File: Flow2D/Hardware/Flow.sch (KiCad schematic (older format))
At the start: 51 parts, among them J1 Conn_02x05_Odd_Even, U1 SN74LVC2G17, U2 LR9102G, U3 TLV9064IDR, U4 STM32G030F6Px

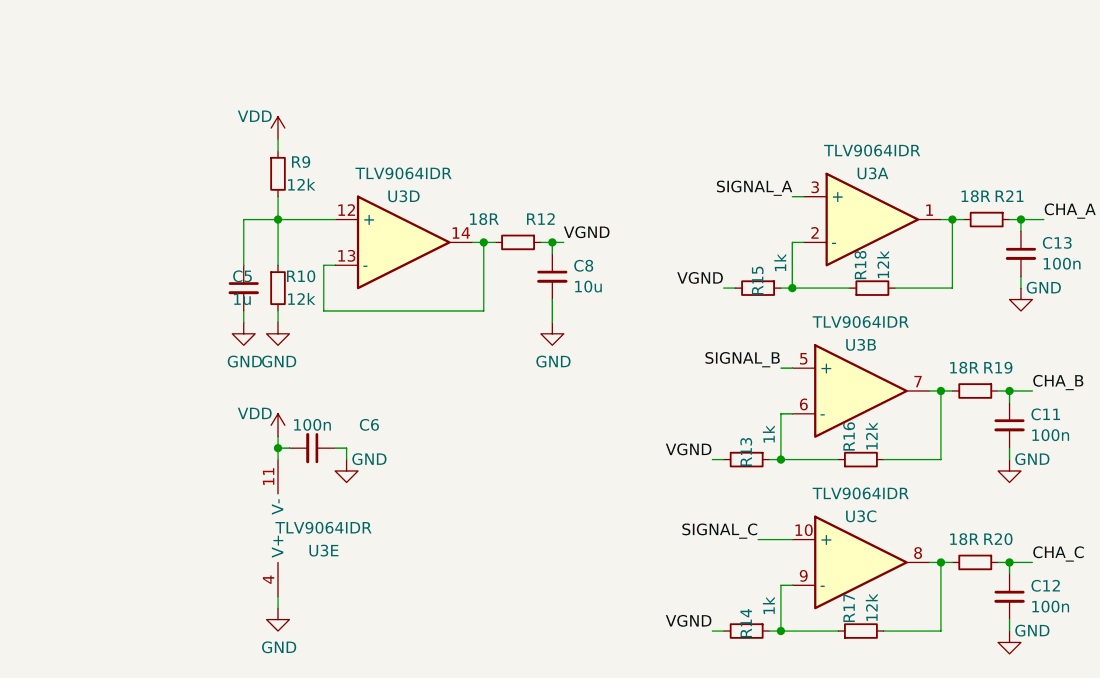
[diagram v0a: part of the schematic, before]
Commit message: Problems related to firmware are solved.
TODO:
+Signal level is too low; like 200mV. Need to be increased.
+Need to be tested with a plastic ring.
+Piezodriver units response is unknown, need to be determined.
+A bit more calculation about vectors required.
+No need for making DMA of the TIM1 active, could be deactivated.
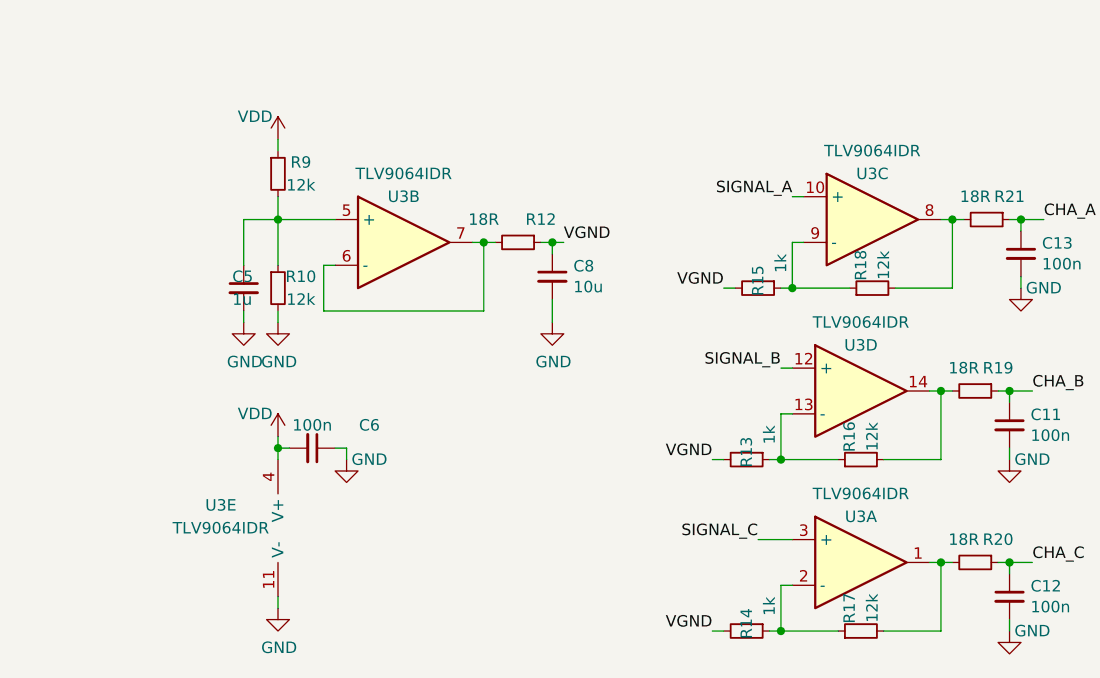
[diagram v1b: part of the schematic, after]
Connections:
- net GND: now also U3.11 (V-); no longer U3.4 (V+)
- net SIGNAL_A: now also U3.10 (+); no longer U3.3 (+)
- net SIGNAL_B: now also U3.12 (+); no longer U3.5 (+)
- net SIGNAL_C: now also U3.3 (+); no longer U3.10 (+)
- net VDD: now also U3.4 (V+); no longer U3.11 (V-)
- net at R16.2, R19.2: now also U3.14; no longer U3.7
- net at R17.2, R20.2: now also U3.1; no longer U3.8
- net at R13.1, R16.1: now also U3.13 (-); no longer U3.6 (-)
- net at R14.1, R17.1: now also U3.2 (-); no longer U3.9 (-)
- net at C5.1, R10.1, R9.2: now also U3.5 (+); no longer U3.12 (+)
- net at R18.2, R21.2: now also U3.8; no longer U3.1
- net at R15.1, R18.1: now also U3.9 (-); no longer U3.2 (-)
- new net: R12.2, U3.6 (-), U3.7
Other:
- moved on the sheet: U3A, U3B, U3C, U3D
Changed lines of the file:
@@
 L Device:Opamp_Quad_Generic U3
 U 4 1 60F6CC8E
-P 6950 7450
-F 0 "U3" H 6950 7650 50  0000 C CNN
-F 1 "TLV9064IDR" H 6950 7750 50  0000 C CNN
-F 2 "Package_SO:SOIC-14_3.9x8.7mm_P1.27mm" H 6950 7450 50  0001 C CNN
-F 3 "~" H 6950 7450 50  0001 C CNN
-F 4 "https://ozdisan.com/entegre-devreler-ics/lineer-entegreler/amplifikatorler/TLV9064IDR" H 6950 7450 50  0001 C CNN "Link"
-F 5 "0.77646" H 6950 7450 50  0001 C CNN "Price"
-	4    6950 7450
+P 8950 8100
+F 0 "U3" H 8950 8300 50  0000 C CNN
+F 1 "TLV9064IDR" H 8950 8400 50  0000 C CNN
+F 2 "Package_SO:SOIC-14_3.9x8.7mm_P1.27mm" H 8950 8100 50  0001 C CNN
+F 3 "~" H 8950 8100 50  0001 C CNN
+F 4 "https://ozdisan.com/entegre-devreler-ics/lineer-entegreler/amplifikatorler/TLV9064IDR" H 8950 8100 50  0001 C CNN "Link"
+F 5 "0.77646" H 8950 8100 50  0001 C CNN "Price"
+	4    8950 8100
 	1    0    0    -1
 $EndComp
@@
 L Device:Opamp_Quad_Generic U3
 U 5 1 60F6DBAD
-P 6500 8700
-F 0 "U3" H 6600 8800 50  0000 C CNN
-F 1 "TLV9064IDR" H 6600 8700 50  0000 C CNN
-F 2 "Package_SO:SOIC-14_3.9x8.7mm_P1.27mm" H 6500 8700 50  0001 C CNN
-F 3 "~" H 6500 8700 50  0001 C CNN
-F 4 "https://ozdisan.com/entegre-devreler-ics/lineer-entegreler/amplifikatorler/TLV9064IDR" H 6500 8700 50  0001 C CNN "Link"
-F 5 "0.77646" H 6500 8700 50  0001 C CNN "Price"
-	5    6500 8700
-	1    0    0    1
+P 6300 8700
+F 0 "U3" H 6450 8800 50  0000 C CNN
+F 1 "TLV9064IDR" H 6450 8700 50  0000 C CNN
+F 2 "Package_SO:SOIC-14_3.9x8.7mm_P1.27mm" H 6300 8700 50  0001 C CNN
+F 3 "~" H 6300 8700 50  0001 C CNN
+F 4 "https://ozdisan.com/entegre-devreler-ics/lineer-entegreler/amplifikatorler/TLV9064IDR" H 6300 8700 50  0001 C CNN "Link"
+F 5 "0.77646" H 6300 8700 50  0001 C CNN "Price"
+	5    6300 8700
+	-1   0    0    -1
 $EndComp
 $Comp
@@
 L Device:Opamp_Quad_Generic U3
 U 1 1 61090EA9
-P 9000 7350
-F 0 "U3" H 9000 7550 50  0000 C CNN
-F 1 "TLV9064IDR" H 9000 7650 50  0000 C CNN
-F 2 "Package_SO:SOIC-14_3.9x8.7mm_P1.27mm" H 9000 7350 50  0001 C CNN
-F 3 "~" H 9000 7350 50  0001 C CNN
-F 4 "https://ozdisan.com/entegre-devreler-ics/lineer-entegreler/amplifikatorler/TLV9064IDR" H 9000 7350 50  0001 C CNN "Link"
-F 5 "0.77646" H 9000 7350 50  0001 C CNN "Price"
-	1    9000 7350
+P 8950 8850
+F 0 "U3" H 8950 9050 50  0000 C CNN
+F 1 "TLV9064IDR" H 8950 9150 50  0000 C CNN
+F 2 "Package_SO:SOIC-14_3.9x8.7mm_P1.27mm" H 8950 8850 50  0001 C CNN
+F 3 "~" H 8950 8850 50  0001 C CNN
+F 4 "https://ozdisan.com/entegre-devreler-ics/lineer-entegreler/amplifikatorler/TLV9064IDR" H 8950 8850 50  0001 C CNN "Link"
+F 5 "0.77646" H 8950 8850 50  0001 C CNN "Price"
+	1    8950 8850
 	1    0    0    -1
 $EndComp
@@
 L Device:Opamp_Quad_Generic U3
 U 2 1 60F6BA2F
-P 8950 8100
-F 0 "U3" H 8950 8300 50  0000 C CNN
-F 1 "TLV9064IDR" H 8950 8400 50  0000 C CNN
-F 2 "Package_SO:SOIC-14_3.9x8.7mm_P1.27mm" H 8950 8100 50  0001 C CNN
-F 3 "~" H 8950 8100 50  0001 C CNN
-F 4 "https://ozdisan.com/entegre-devreler-ics/lineer-entegreler/amplifikatorler/TLV9064IDR" H 8950 8100 50  0001 C CNN "Link"
-F 5 "0.77646" H 8950 8100 50  0001 C CNN "Price"
-	2    8950 8100
+P 6950 7450
+F 0 "U3" H 6950 7650 50  0000 C CNN
+F 1 "TLV9064IDR" H 6950 7750 50  0000 C CNN
+F 2 "Package_SO:SOIC-14_3.9x8.7mm_P1.27mm" H 6950 7450 50  0001 C CNN
+F 3 "~" H 6950 7450 50  0001 C CNN
+F 4 "https://ozdisan.com/entegre-devreler-ics/lineer-entegreler/amplifikatorler/TLV9064IDR" H 6950 7450 50  0001 C CNN "Link"
+F 5 "0.77646" H 6950 7450 50  0001 C CNN "Price"
+	2    6950 7450
 	1    0    0    -1
 $EndComp
@@
 L Device:Opamp_Quad_Generic U3
 U 3 1 60F6C53B
-P 8950 8850
-F 0 "U3" H 8950 9050 50  0000 C CNN
-F 1 "TLV9064IDR" H 8950 9150 50  0000 C CNN
-F 2 "Package_SO:SOIC-14_3.9x8.7mm_P1.27mm" H 8950 8850 50  0001 C CNN
-F 3 "~" H 8950 8850 50  0001 C CNN
-F 4 "https://ozdisan.com/entegre-devreler-ics/lineer-entegreler/amplifikatorler/TLV9064IDR" H 8950 8850 50  0001 C CNN "Link"
-F 5 "0.77646" H 8950 8850 50  0001 C CNN "Price"
-	3    8950 8850
-	1    0    0    -1
-$EndComp
+P 9000 7350
+F 0 "U3" H 9000 7550 50  0000 C CNN
+F 1 "TLV9064IDR" H 9000 7650 50  0000 C CNN
+F 2 "Package_SO:SOIC-14_3.9x8.7mm_P1.27mm" H 9000 7350 50  0001 C CNN
+F 3 "~" H 9000 7350 50  0001 C CNN
+F 4 "https://ozdisan.com/entegre-devreler-ics/lineer-entegreler/amplifikatorler/TLV9064IDR" H 9000 7350 50  0001 C CNN "Link"
+F 5 "0.77646" H 9000 7350 50  0001 C CNN "Price"
+	3    9000 7350
+	1    0    0    -1
+$EndComp
